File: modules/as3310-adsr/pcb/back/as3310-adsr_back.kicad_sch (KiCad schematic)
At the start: 23 parts

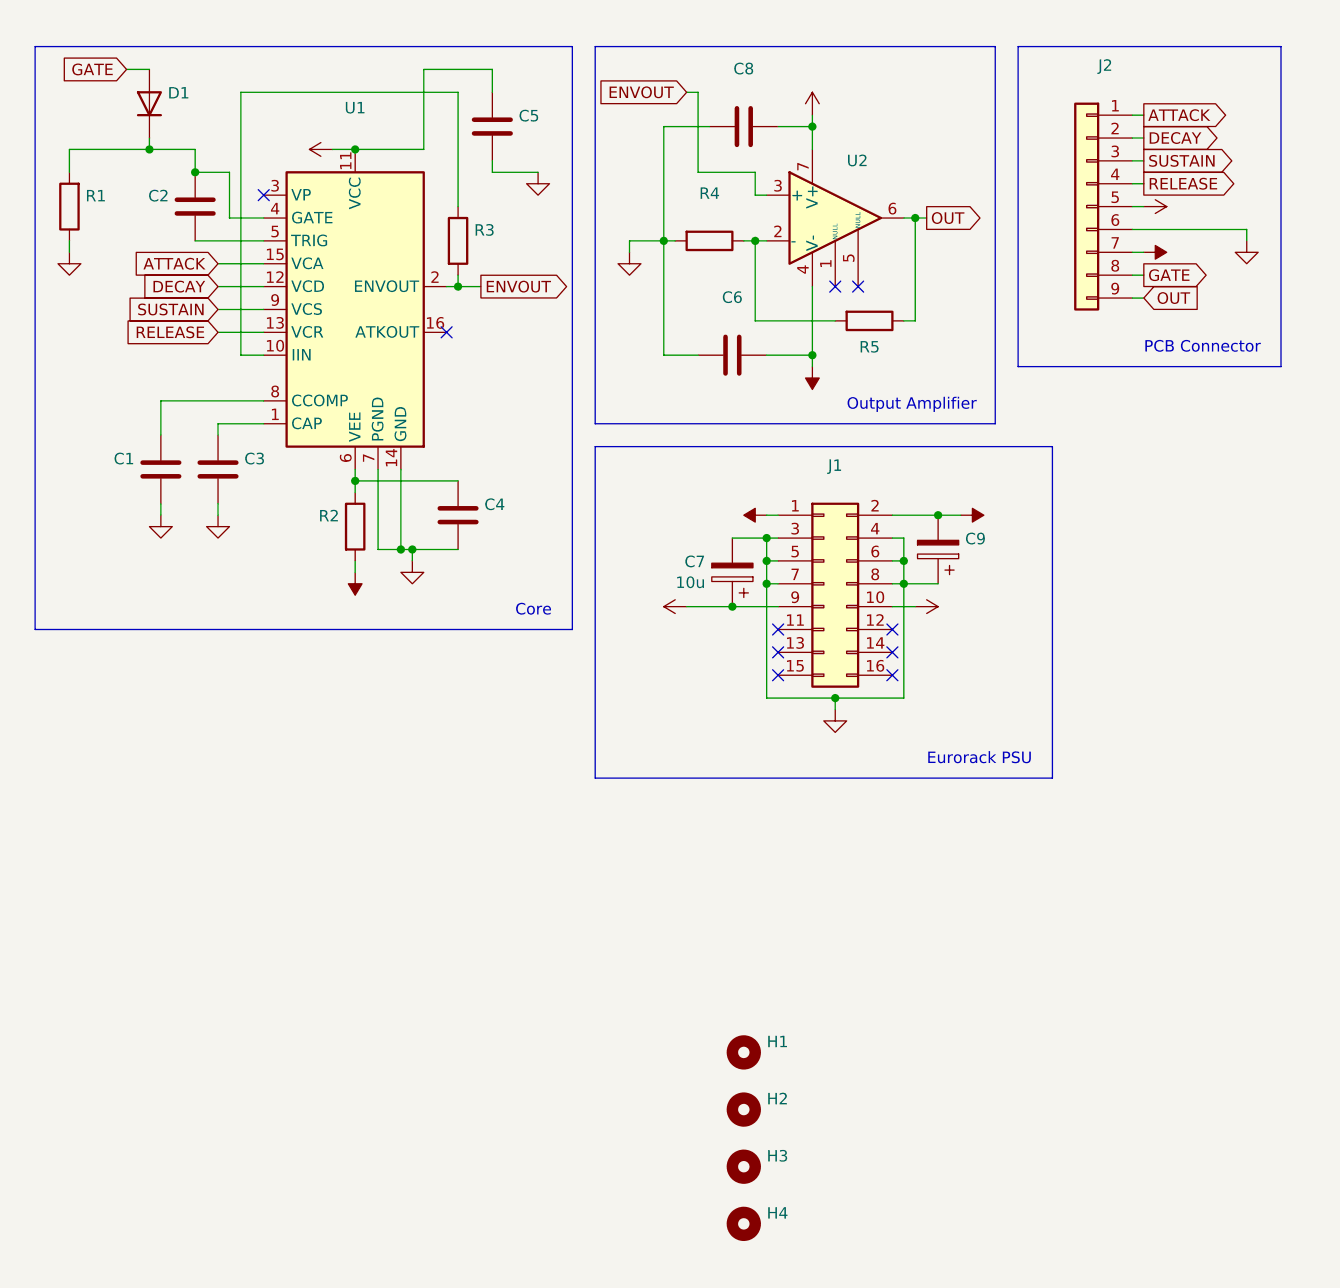
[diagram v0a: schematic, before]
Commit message: modules: as3310-adsr: back: revision A (redesign)
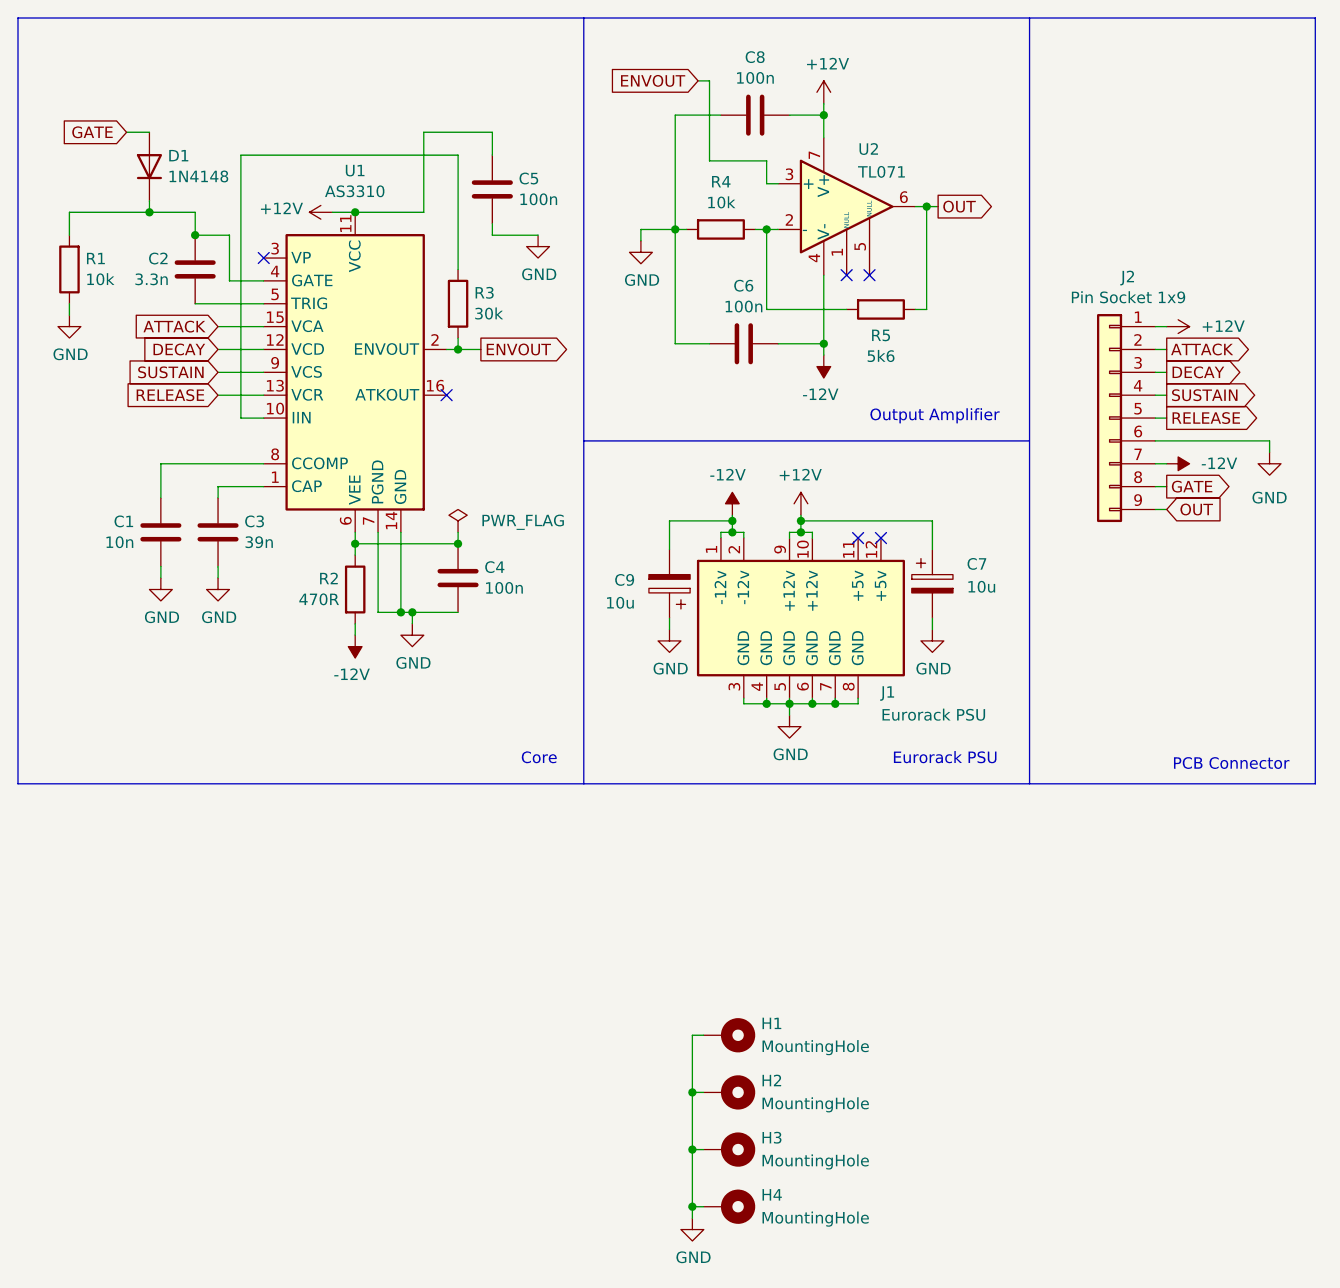
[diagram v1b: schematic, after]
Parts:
- removed J1: (no value), symbol Connector_Generic:Conn_02x08_Odd_Even
- added J1: Eurorack PSU, eurorack:IDC-Header_2x08_P2.54mm_Vertical, symbol eurorack:Connector_Eurorack_PSU
- C1: value (none) -> 10n; footprint (none) -> Capacitor_THT:C_Disc_D3.0mm_W1.6mm_P2.50mm
- C2: value (none) -> 3.3n; footprint (none) -> Capacitor_THT:C_Disc_D3.0mm_W1.6mm_P2.50mm
- C3: value (none) -> 39n; footprint (none) -> Capacitor_THT:C_Rect_L13.0mm_W5.0mm_P10.00mm_FKS3_FKP3_MKS4
- C4, C5, C6, C8: value (none) -> 100n; footprint (none) -> Capacitor_THT:C_Disc_D4.3mm_W1.9mm_P5.00mm
- C9: value (none) -> 10u; footprint (none) -> Capacitor_THT:CP_Radial_D5.0mm_P2.50mm
- D1: value (none) -> 1N4148; footprint (none) -> Diode_THT:D_DO-35_SOD27_P7.62mm_Horizontal
- H1, H2, H3, H4: value (none) -> MountingHole; footprint (none) -> MountingHole:MountingHole_2.2mm_M2_Pad_Via; symbol Mechanical:MountingHole -> Mechanical:MountingHole_Pad
- J2: value (none) -> Pin Socket 1x9; footprint (none) -> Connector_PinSocket_2.54mm:PinSocket_1x09_P2.54mm_Vertical
- R1, R4: value (none) -> 10k; footprint (none) -> Resistor_THT:R_Axial_DIN0207_L6.3mm_D2.5mm_P10.16mm_Horizontal
- R2: value (none) -> 470R; footprint (none) -> Resistor_THT:R_Axial_DIN0207_L6.3mm_D2.5mm_P10.16mm_Horizontal
- R3: value (none) -> 30k; footprint (none) -> Resistor_THT:R_Axial_DIN0207_L6.3mm_D2.5mm_P10.16mm_Horizontal
- R5: value (none) -> 5k6; footprint (none) -> Resistor_THT:R_Axial_DIN0207_L6.3mm_D2.5mm_P10.16mm_Horizontal
- U1: value (none) -> AS3310; footprint (none) -> Package_DIP:DIP-16_W7.62mm
- U2: value (none) -> TL071; footprint (none) -> Package_DIP:DIP-8_W7.62mm
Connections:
- net +12V: now also J2.1 (Pin_1), J1.10 (+12v), J1.9 (+12v); no longer J2.5 (Pin_5)
- net -12V: now also J1.1 (-12v), J1.2 (-12v)
- net ATTACK: now also J2.2 (Pin_2); no longer J2.1 (Pin_1)
- net DECAY: now also J2.3 (Pin_3); no longer J2.2 (Pin_2)
- net GND: now also H1.1, H2.1, H3.1, H4.1, J1.3 (GND), J1.4 (GND), J1.5 (GND), J1.6 (GND), J1.7 (GND), J1.8 (GND)
- net RELEASE: now also J2.5 (Pin_5); no longer J2.4 (Pin_4)
- net SUSTAIN: now also J2.4 (Pin_4); no longer J2.3 (Pin_3)
- no-connect marks 10 -> 6
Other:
- company: (none) -> eurorack.rgm.io
- moved on the sheet: C1, C2, C3, C4, C5, C6, C7, C8, C9, D1, J2, R1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
